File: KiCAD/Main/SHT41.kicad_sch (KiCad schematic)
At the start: 4 parts, among them U12 SHT4x

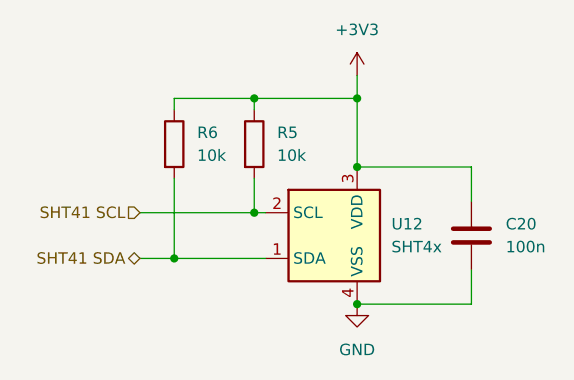
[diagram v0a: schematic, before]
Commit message: Create wiring diagram draft
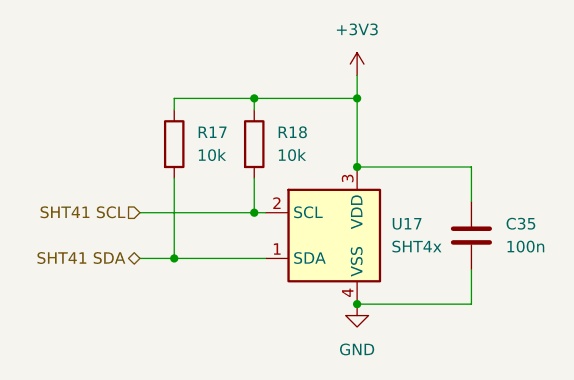
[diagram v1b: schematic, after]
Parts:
- renumbered C20 to C35, R6 to R17, R5 to R18, U12 to U17
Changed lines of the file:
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@@
 		(dnp no)
 		(fields_autoplaced yes)
-		(property "Reference" "#PWR040"
+		(property "Reference" "#PWR061"
 			(at 127 69.85 0)
 			(effects
@@
 			(project ""
 				(path "/bbb10697-a5dd-43b8-9c6f-4c5919cf3463/896d693a-fbbd-418a-ac8a-f8826c549ae5"
-					(reference "#PWR040")
+					(reference "#PWR061")
 					(unit 1)
 				)
@@
 		(dnp no)
 		(fields_autoplaced yes)
-		(property "Reference" "R5"
+		(property "Reference" "R18"
 			(at 118.11 72.39 0)
 			(effects
@@
 			(project ""
 				(path "/bbb10697-a5dd-43b8-9c6f-4c5919cf3463/896d693a-fbbd-418a-ac8a-f8826c549ae5"
-					(reference "R5")
+					(reference "R18")
 					(unit 1)
 				)
@@
 		(dnp no)
 		(fields_autoplaced yes)
-		(property "Reference" "U12"
+		(property "Reference" "U17"
 			(at 130.81 82.55 0)
 			(effects
@@
 			(project ""
 				(path "/bbb10697-a5dd-43b8-9c6f-4c5919cf3463/896d693a-fbbd-418a-ac8a-f8826c549ae5"
-					(reference "U12")
+					(reference "U17")
 					(unit 1)
 				)
@@
 		(dnp no)
 		(fields_autoplaced yes)
-		(property "Reference" "C20"
+		(property "Reference" "C35"
 			(at 143.51 82.55 0)
 			(effects
@@
 			(project ""
 				(path "/bbb10697-a5dd-43b8-9c6f-4c5919cf3463/896d693a-fbbd-418a-ac8a-f8826c549ae5"
-					(reference "C20")
+					(reference "C35")
 					(unit 1)
 				)
@@
 		(dnp no)
 		(fields_autoplaced yes)
-		(property "Reference" "R6"
+		(property "Reference" "R17"
 			(at 109.22 72.39 0)
 			(effects
@@
 			(project "Main"
 				(path "/bbb10697-a5dd-43b8-9c6f-4c5919cf3463/896d693a-fbbd-418a-ac8a-f8826c549ae5"
-					(reference "R6")
+					(reference "R17")
 					(unit 1)
 				)
@@
 		(dnp no)
 		(fields_autoplaced yes)
-		(property "Reference" "#PWR041"
+		(property "Reference" "#PWR062"
 			(at 127 97.79 0)
 			(effects
@@
 			(project ""
 				(path "/bbb10697-a5dd-43b8-9c6f-4c5919cf3463/896d693a-fbbd-418a-ac8a-f8826c549ae5"
-					(reference "#PWR041")
-					(unit 1)
-				)
+					(reference "#PWR062")
+					(unit 1)
+				)

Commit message: Update RF sys and footprints
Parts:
- C35: footprint (none) -> Capacitor_SMD:C_0603_1608Metric
- R17, R18: footprint (none) -> Resistor_SMD:R_0603_1608Metric
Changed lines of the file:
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@@
 			)
 		)
-		(property "Footprint" ""
+		(property "Footprint" "Resistor_SMD:R_0603_1608Metric"
 			(at 113.792 73.66 90)
 			(effects
@@
 			)
 		)
-		(property "Footprint" ""
+		(property "Footprint" "Capacitor_SMD:C_0603_1608Metric"
 			(at 140.6652 87.63 0)
 			(effects
@@
 			)
 		)
-		(property "Footprint" ""
+		(property "Footprint" "Resistor_SMD:R_0603_1608Metric"
 			(at 104.902 73.66 90)
 			(effects
